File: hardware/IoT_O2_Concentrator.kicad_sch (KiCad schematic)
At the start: 4 parts, among them J1 ESP32_R, J2 SIM_GSM_EVB, J3 LCD_20x04, J4 ESP32_R

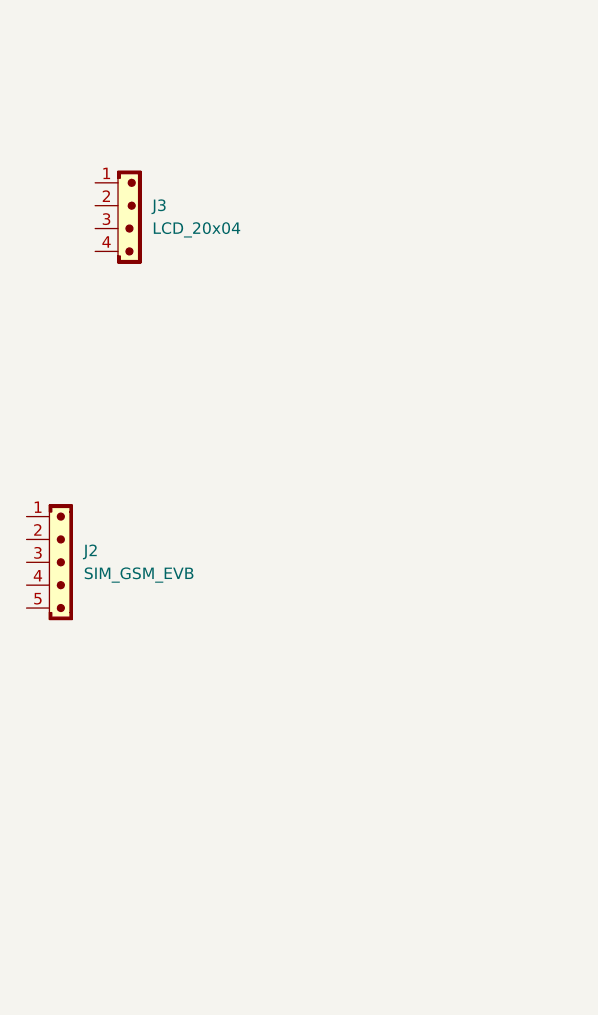
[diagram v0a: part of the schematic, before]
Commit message: Snapping to grid errors
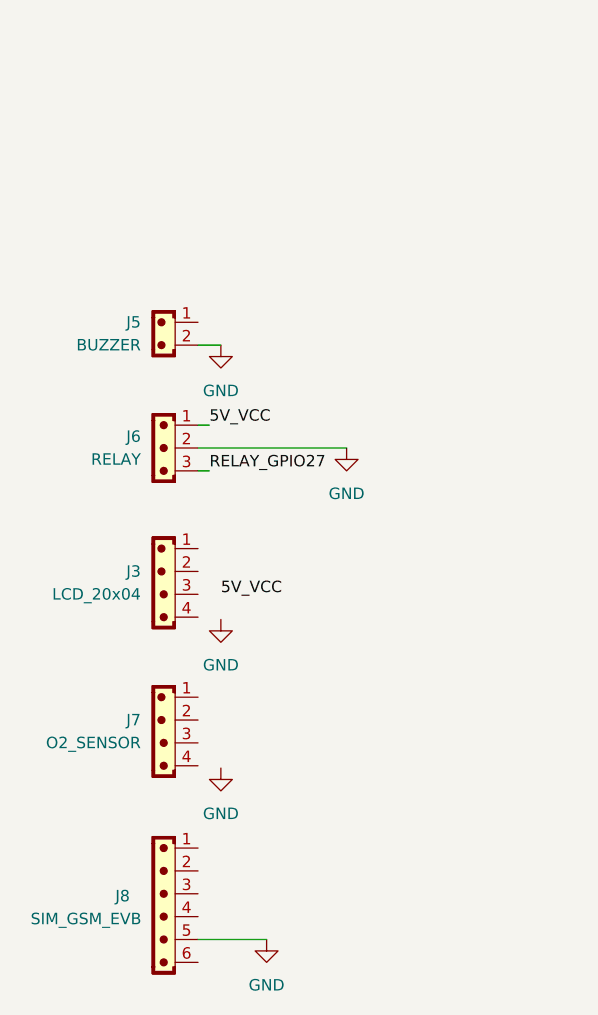
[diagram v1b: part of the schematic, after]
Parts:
- removed J2: SIM_GSM_EVB, Connector_JST:JST_EH_B5B-EH-A_1x05_P2.50mm_Vertical, symbol PCM_SL_Connectors:JST_05
- added J5: BUZZER, Connector_JST:JST_EH_B2B-EH-A_1x02_P2.50mm_Vertical, symbol PCM_SL_Connectors:JST_02
- added J6: RELAY, Connector_JST:JST_EH_B3B-EH-A_1x03_P2.50mm_Vertical, symbol PCM_SL_Connectors:JST_03
- added J7: O2_SENSOR, Connector_JST:JST_EH_B4B-EH-A_1x04_P2.50mm_Vertical, symbol PCM_SL_Connectors:JST_04
- added J8: SIM_GSM_EVB, Connector_JST:JST_EH_B6B-EH-A_1x06_P2.50mm_Vertical, symbol PCM_SL_Connectors:JST_06
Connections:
- new net 5V_VCC: J6.1
- new net GND: J5.2, J6.2, J8.5
- new net RELAY_GPIO27: J6.3
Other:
- moved on the sheet: J3

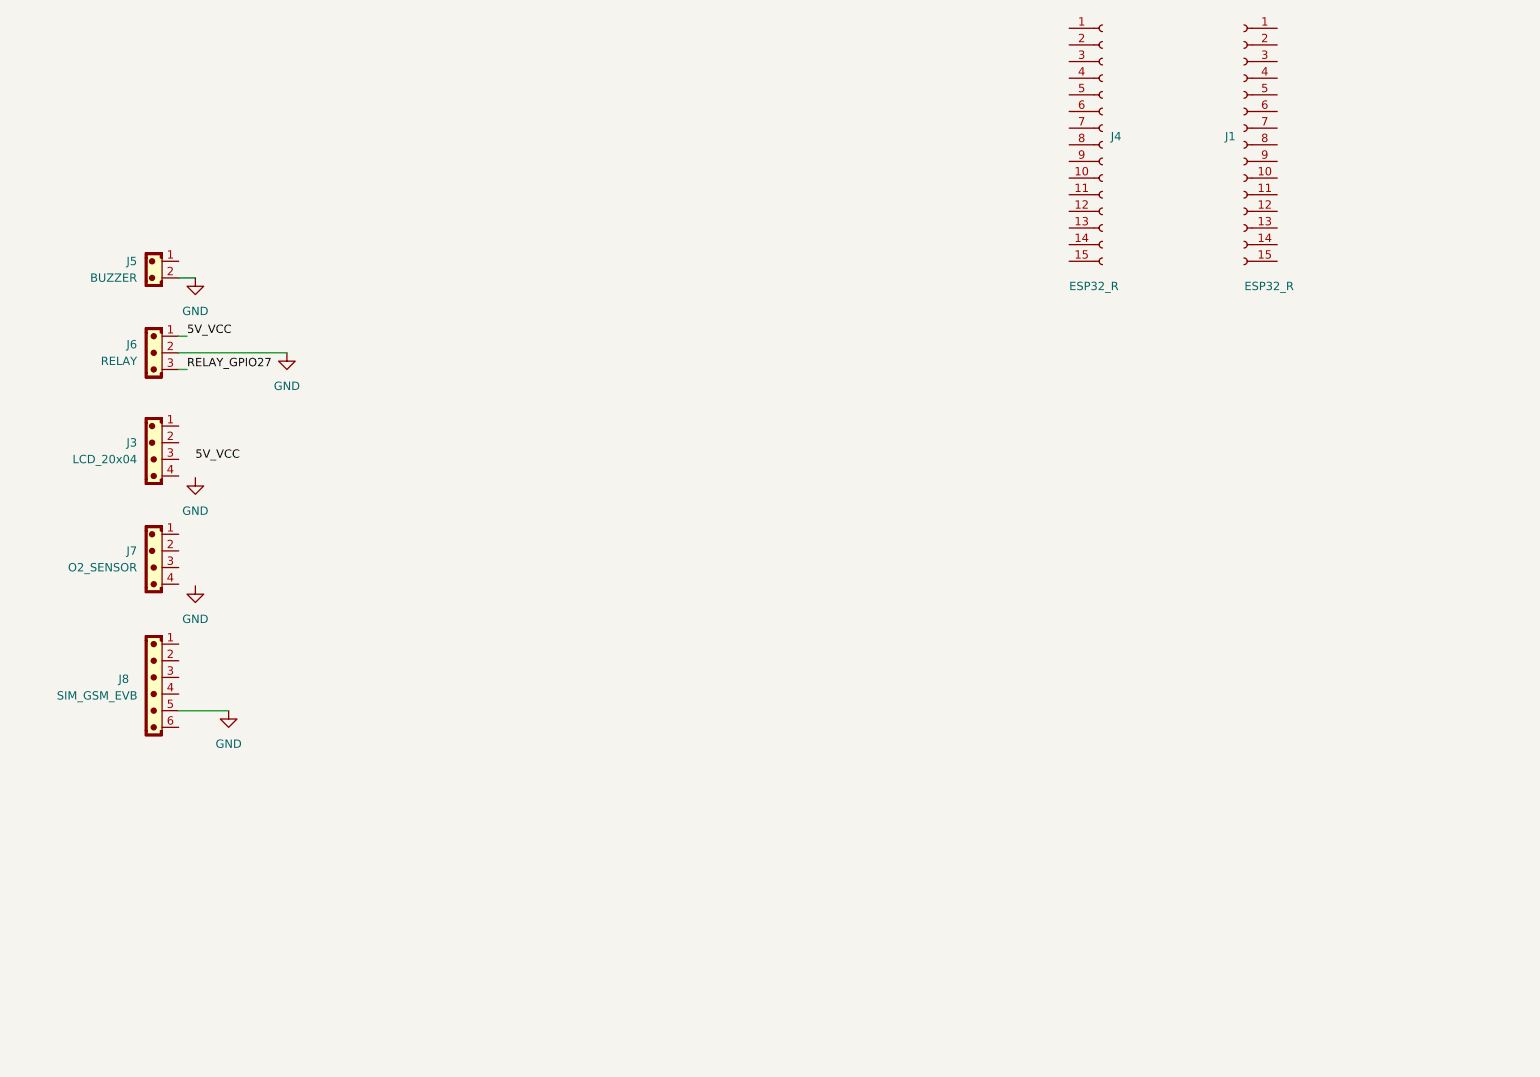
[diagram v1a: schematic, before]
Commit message: Started PCB routing
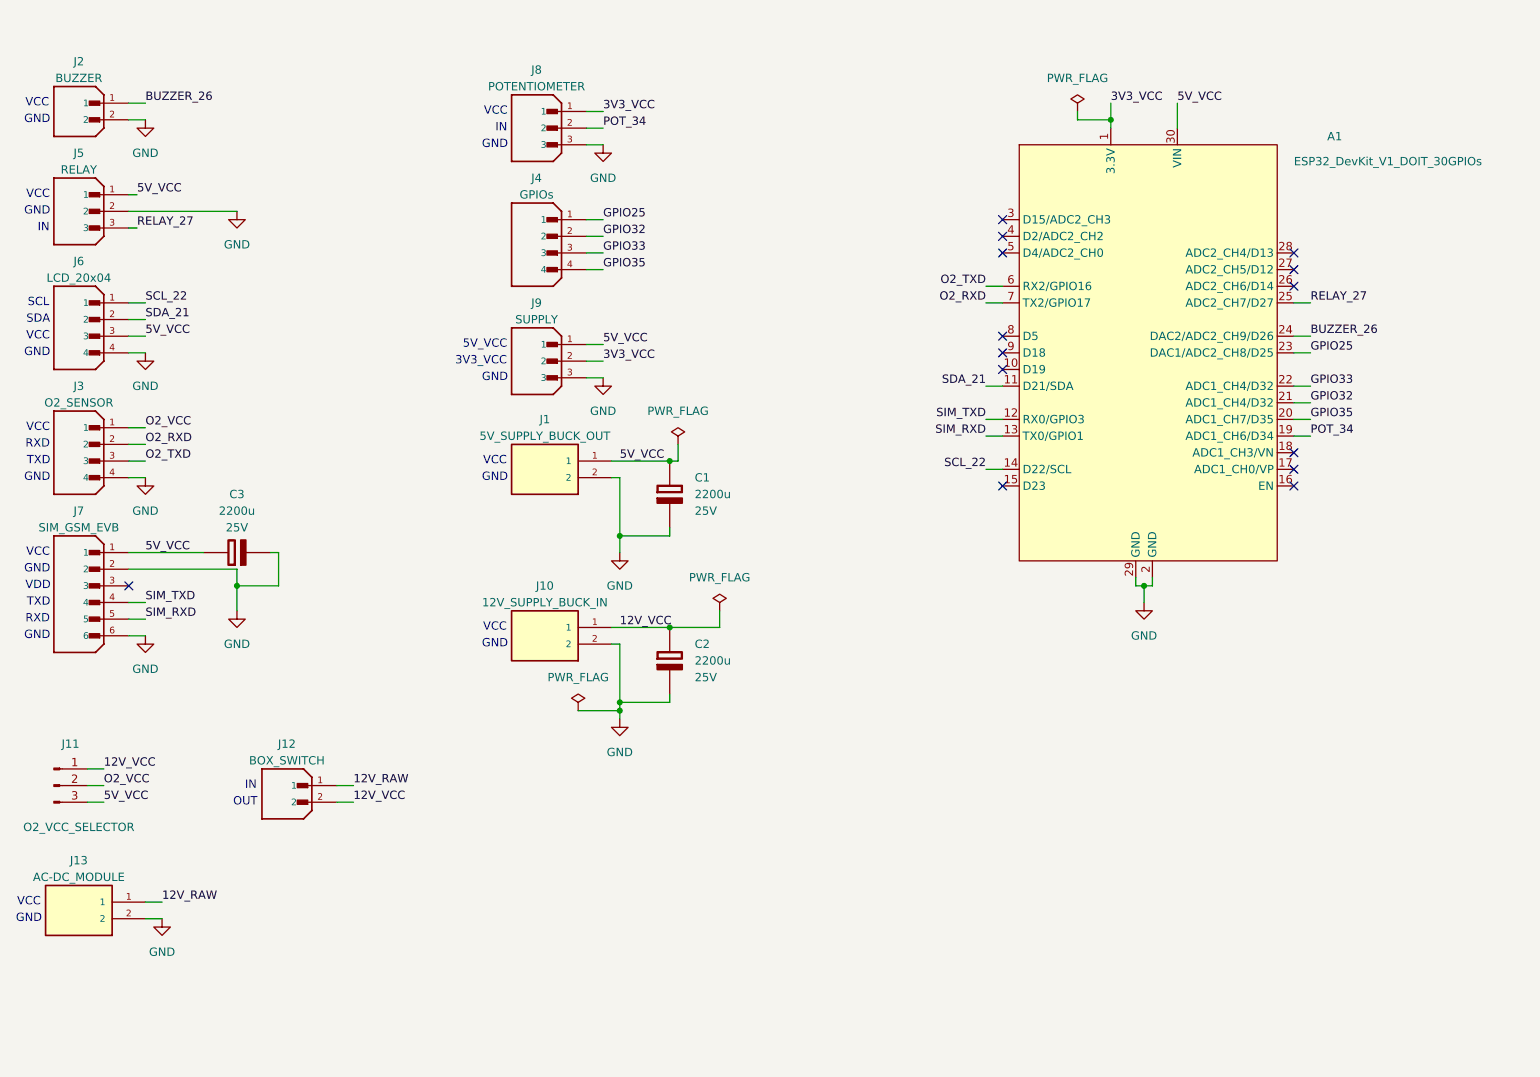
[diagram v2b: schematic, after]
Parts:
- removed J1, J4: ESP32_R, symbol Connector:Conn_01x15_Socket
- removed J3: LCD_20x04, Connector_JST:JST_EH_B4B-EH-A_1x04_P2.50mm_Vertical, symbol PCM_SL_Connectors:JST_04
- removed J5: BUZZER, Connector_JST:JST_EH_B2B-EH-A_1x02_P2.50mm_Vertical, symbol PCM_SL_Connectors:JST_02
- removed J6: RELAY, Connector_JST:JST_EH_B3B-EH-A_1x03_P2.50mm_Vertical, symbol PCM_SL_Connectors:JST_03
- removed J7: O2_SENSOR, Connector_JST:JST_EH_B4B-EH-A_1x04_P2.50mm_Vertical, symbol PCM_SL_Connectors:JST_04
- removed J8: SIM_GSM_EVB, Connector_JST:JST_EH_B6B-EH-A_1x06_P2.50mm_Vertical, symbol PCM_SL_Connectors:JST_06
- added A1: ESP32_DevKit_V1_DOIT_30GPIOs, PCM_SL_Development_Boards:DOIT_ESP32_DEVKIT_30Pins, symbol PCM_SL_Development_Board:ESP32_DevKit_V1_DOIT_30GPIOs
- added C1, C2, C3: 2200u, Capacitor_THT:C_Radial_D10.0mm_H20.0mm_P5.00mm, symbol PCM_Elektuur:C-polar
- added J1: 5V_SUPPLY_BUCK_OUT, footprint:TB002-500-02BE, symbol TB002-500-02BE:TB002-500-02BE
- added J10: 12V_SUPPLY_BUCK_IN, footprint:TB002-500-02BE, symbol TB002-500-02BE:TB002-500-02BE
- added J11: O2_VCC_SELECTOR, Connector_PinHeader_2.54mm:PinHeader_1x03_P2.54mm_Vertical, symbol Connector:Conn_01x03_Pin
- added J12: BOX_SWITCH, footprint:JST_B2B-XH-A, symbol B2B-XH-A:B2B-XH-A
- added J13: AC-DC_MODULE, footprint:TB002-500-02BE, symbol TB002-500-02BE:TB002-500-02BE
- added J2: BUZZER, footprint:JST_B2B-XH-A, symbol B2B-XH-A:B2B-XH-A
- added J3: O2_SENSOR, footprint:JST_B4B-XH-A, symbol B4B-XH-A:B4B-XH-A
- added J4: GPIOs, footprint:JST_B4B-XH-A, symbol B4B-XH-A:B4B-XH-A
- added J5: RELAY, footprint:JST_B3B-XH-A, symbol B3B-XH-A:B3B-XH-A
- added J6: LCD_20x04, footprint:JST_B4B-XH-A, symbol B4B-XH-A:B4B-XH-A
- added J7: SIM_GSM_EVB, footprint:JST_B6B-XH-A, symbol B6B-XH-A:B6B-XH-A
- added J8: POTENTIOMETER, footprint:JST_B3B-XH-A, symbol B3B-XH-A:B3B-XH-A
- added J9: SUPPLY, footprint:JST_B3B-XH-A, symbol B3B-XH-A:B3B-XH-A
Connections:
- net 5V_VCC: now also A1.30 (VIN), C1.1 (+), C3.1 (+), J1.1, J11.3 (Pin_3), J5.1, J6.3, J7.1, J9.1
- net GND: now also A1.2 (GND), A1.29 (GND), C1.2 (-), C2.2 (-), C3.2 (-), J1.2, J10.2, J13.2, J2.2, J3.4, J5.2, J6.4, J7.2, J7.6, J8.3, J9.3
- new net 12V_RAW: J12.1, J13.1
- new net 12V_VCC: C2.1 (+), J10.1, J11.1 (Pin_1), J12.2
- new net 3V3_VCC: A1.1 (3.3V), J8.1, J9.2
- new net BUZZER_26: A1.24 (DAC2/ADC2_CH9/D26), J2.1
- new net GPIO25: A1.23 (DAC1/ADC2_CH8/D25), J4.1
- new net GPIO32: A1.21 (ADC1_CH4/D32), J4.2
- new net GPIO33: A1.22 (ADC1_CH4/D32), J4.3
- new net GPIO35: A1.20 (ADC1_CH7/D35), J4.4
- new net O2_RXD: A1.7 (TX2/GPIO17), J3.2
- new net O2_TXD: A1.6 (RX2/GPIO16), J3.3
- new net O2_VCC: J11.2 (Pin_2), J3.1
- new net POT_34: A1.19 (ADC1_CH6/D34), J8.2
- new net RELAY_27: A1.25 (ADC2_CH7/D27), J5.3
- new net SCL_22: A1.14 (D22/SCL), J6.1
- new net SDA_21: A1.11 (D21/SDA), J6.2
- new net SIM_RXD: A1.13 (TX0/GPIO1), J7.5
- new net SIM_TXD: A1.12 (RX0/GPIO3), J7.4
- no-connect marks 0 -> 14
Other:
- note added: "3V3_VCC"
- note added: "5V_VCC"
- note added: "GND"
- note added: "IN"
- note added: "OUT"
- note added: "RXD"
- note added: "SCL"
- note added: "SDA"
- note added: "TXD"
- note added: "VCC"
- note added: "VDD"
- company: (none) -> BigSmartt
- title: (none) -> IoT_O2_Concentrator

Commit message: Finishing the routing
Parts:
- added JP1: 5V_JUMPER, PCM_Jumper_AKL:Jumper_P7.62mm_D1.2mm, symbol Jumper:Jumper_2_Bridged
- added JP2: GND_JUMPER, PCM_Jumper_AKL:Jumper_P7.62mm_D1.2mm, symbol Jumper:Jumper_2_Bridged
- added JP3: 5V_JUMPER, PCM_Jumper_AKL:Jumper_P10.16mm_D1.2mm, symbol Jumper:Jumper_2_Bridged
- added JP4: 5V_JUMPER, PCM_Jumper_AKL:Jumper_P5.08mm_D1.2mm, symbol Jumper:Jumper_2_Bridged
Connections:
- net 5V_VCC: now also JP1.1 (A), JP1.2 (B), JP3.1 (A), JP3.2 (B), JP4.1 (A), JP4.2 (B)
- net GND: now also JP2.1 (A), JP2.2 (B)
- net GPIO32: now also J4.3; no longer J4.2
- net GPIO33: now also J4.2; no longer J4.3

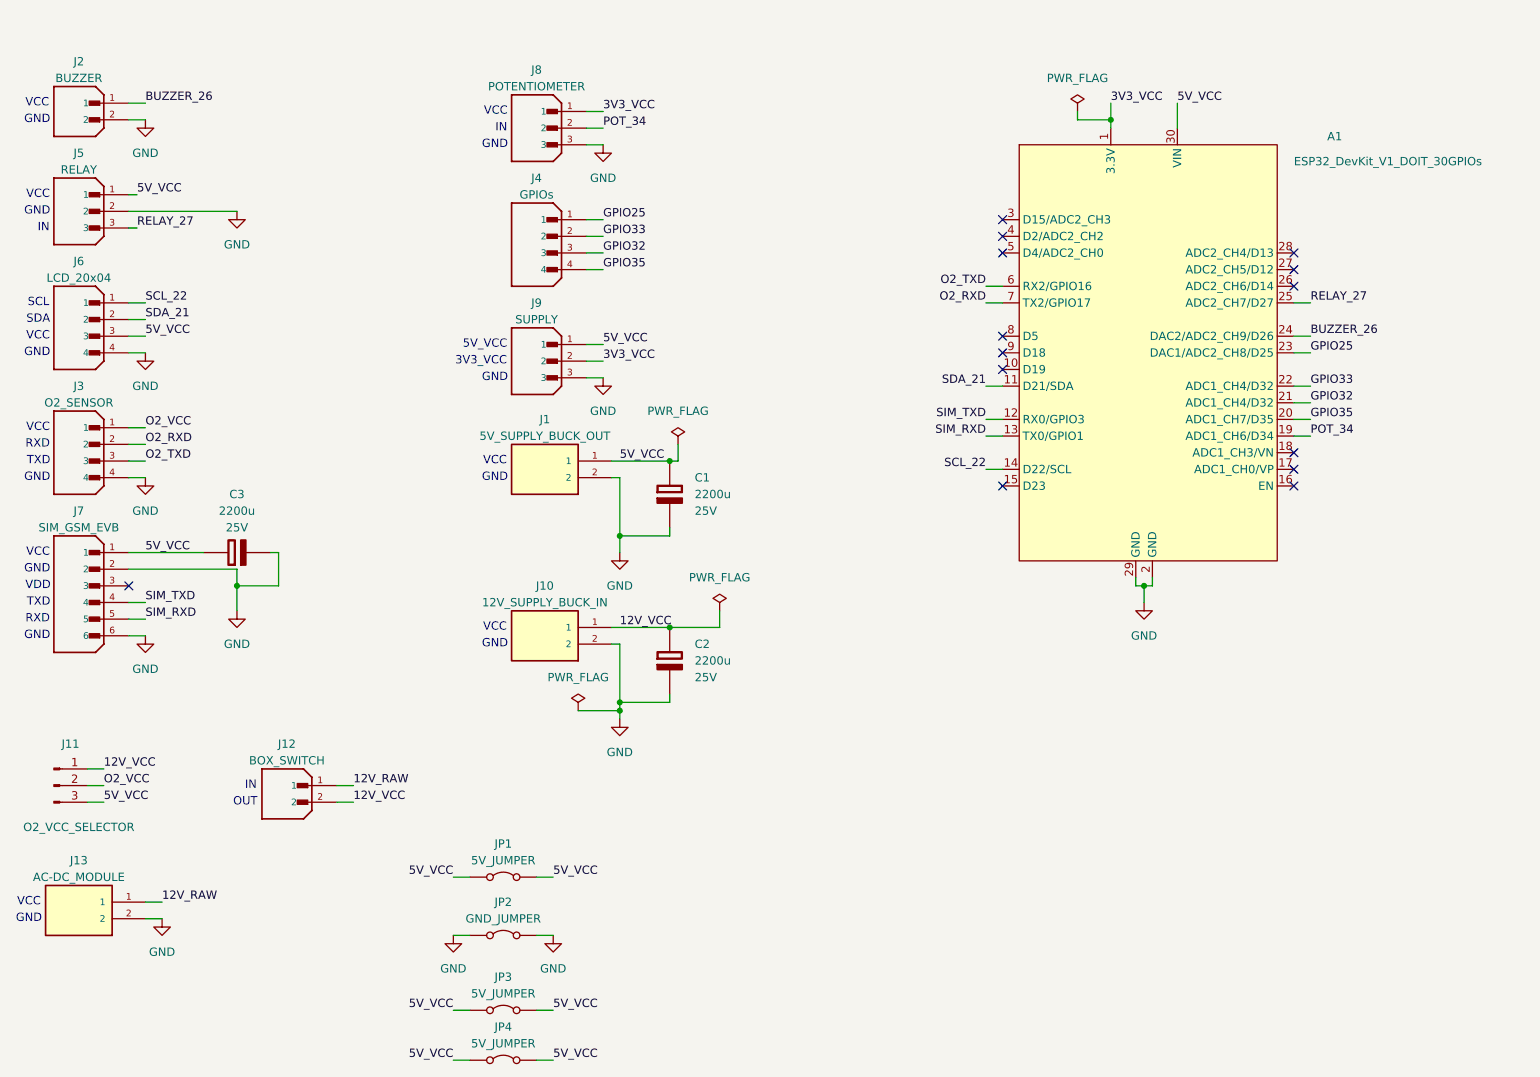
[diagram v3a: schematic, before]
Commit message: Routing with correct SIM tx/rx & labelling
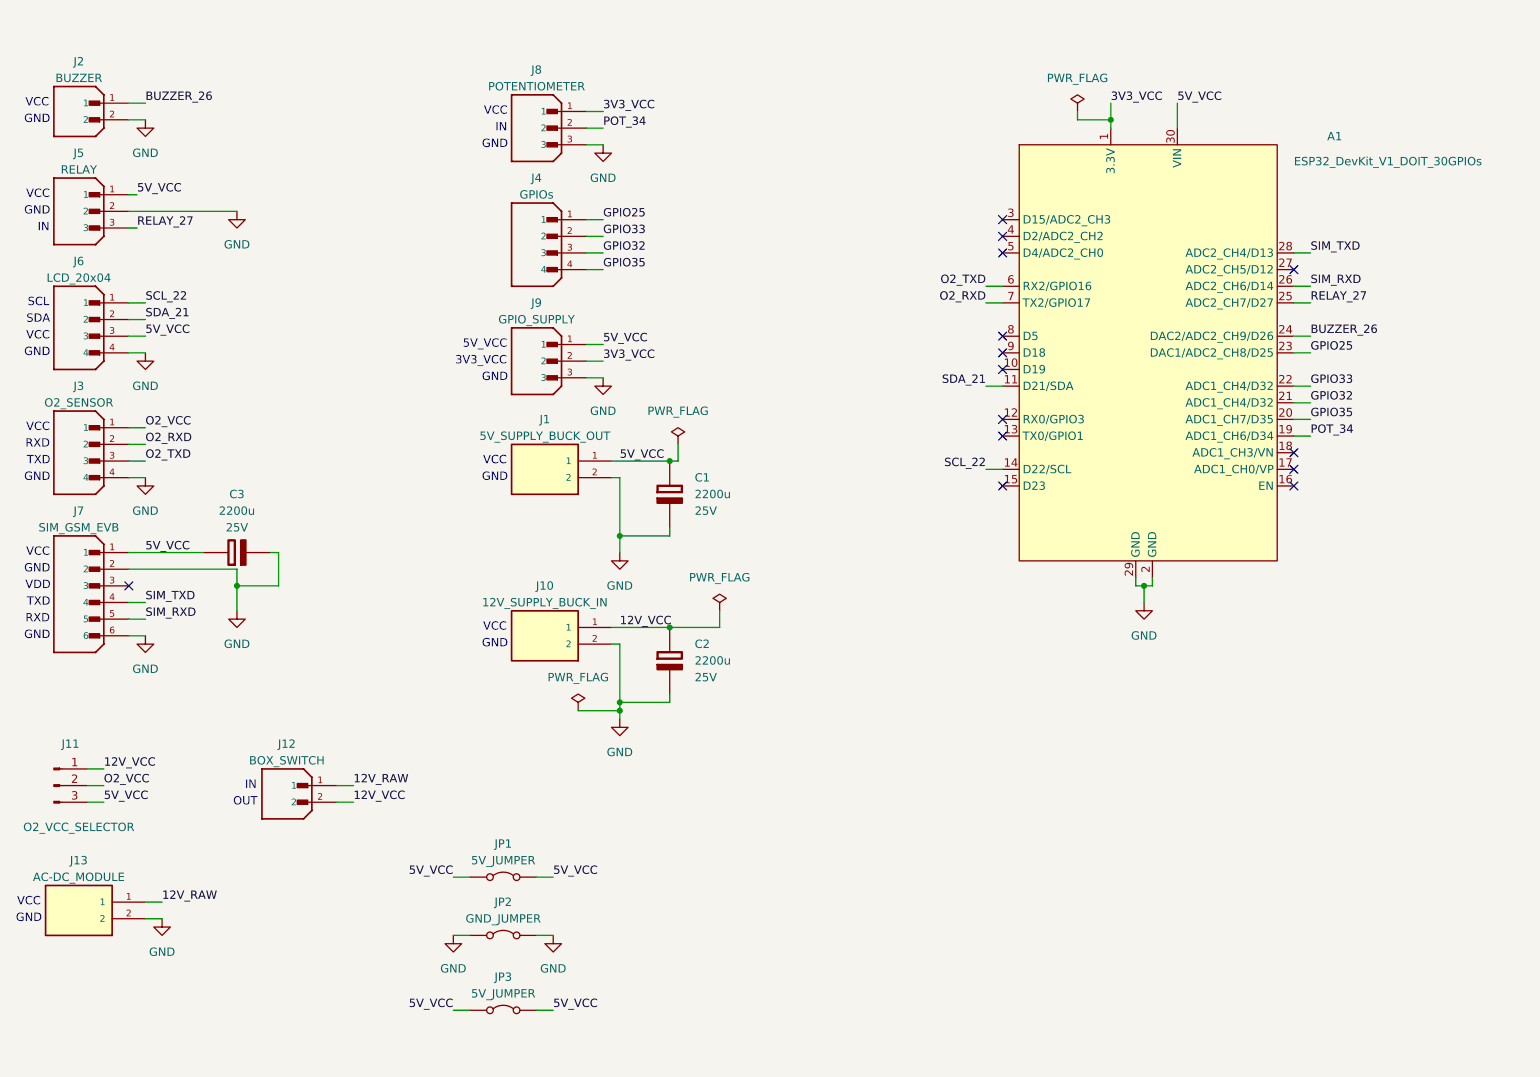
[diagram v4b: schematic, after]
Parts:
- removed JP4: 5V_JUMPER, PCM_Jumper_AKL:Jumper_P5.08mm_D1.2mm, symbol Jumper:Jumper_2_Bridged
- J9: value SUPPLY -> GPIO_SUPPLY
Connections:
- net SIM_RXD: now also A1.26 (ADC2_CH6/D14); no longer A1.13 (TX0/GPIO1)
- net SIM_TXD: now also A1.28 (ADC2_CH4/D13); no longer A1.12 (RX0/GPIO3)

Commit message: PCB Routing completed
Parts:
- A1: value ESP32_DevKit_V1_DOIT_30GPIOs -> ESP32_DevKit
- C1, C2, C3: footprint Capacitor_THT:C_Radial_D10.0mm_H20.0mm_P5.00mm -> Capacitor_THT:C_Radial_D10.0mm_H12.5mm_P5.00mm
- J1: value 5V_SUPPLY_BUCK_OUT -> 5V_BUCK_OUT
- J10: value 12V_SUPPLY_BUCK_IN -> 12V_BUCK_IN
- J11: value O2_VCC_SELECTOR -> O2_VCC_SEL
- J13: value AC-DC_MODULE -> DC_MODULE

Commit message: Corrected the firmware and added the O2 data derivation
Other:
- company: BigSmartt -> ---
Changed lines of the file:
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@@
 		(date "2026-06-24")
 		(rev "1.0")
-		(company "BigSmartt")
+		(company "---")
 	)
